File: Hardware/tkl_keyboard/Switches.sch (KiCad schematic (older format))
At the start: 178 parts, among them SW10 K33, SW11 K49, SW12 K64, SW13 K2, SW14 K18, SW15 K34, SW16 K50, SW17 K65, SW18 K78, SW19 K3, SW2 K0, SW20 K19, SW21 K35, SW22 K51, SW23 K66, SW24 K4, SW25 K20, SW26 K36, SW27 K52, SW28 K67, SW29 K79, SW3 K16, SW30 K5, SW31 K21, SW32 K37, SW33 K53, SW34 K68, SW35 K6, SW36 K22, SW37 K38, SW38 K54, SW39 K69, SW4 K32, SW40 K80, SW41 K7, SW42 K23, SW43 K39, SW44 K55, SW45 K70, SW46 K8, SW47 K24, SW48 K40, SW49 K56, SW5 K48, SW50 K71, SW51 K81, SW52 K9, SW53 K25, SW54 K41, SW55 K57, SW56 K72, SW57 K82, SW58 K10, SW59 K26, SW6 K63, SW60 K42, SW61 K58, SW62 K73, SW63 K83, SW64 K11, SW65 K27, SW66 K43, SW67 K59, SW68 K74, SW69 K84, SW7 K77, SW70 K12, SW71 K28, SW72 K44, SW73 K60, SW74 K75, SW75 K85, SW76 K13, SW77 K29, SW78 K45, SW79 K61, SW8 K1, SW80 K86, SW81 K14, SW82 K30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

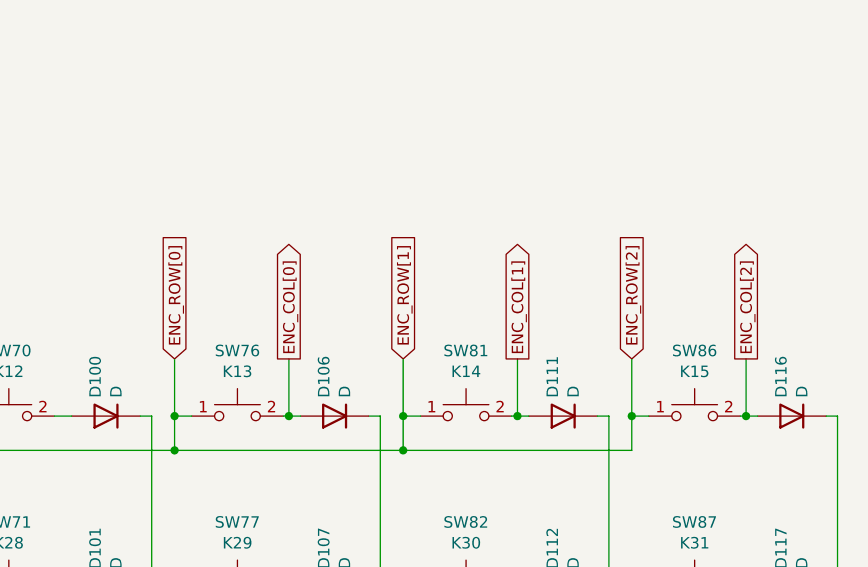
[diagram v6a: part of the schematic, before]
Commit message: Tidying schematic
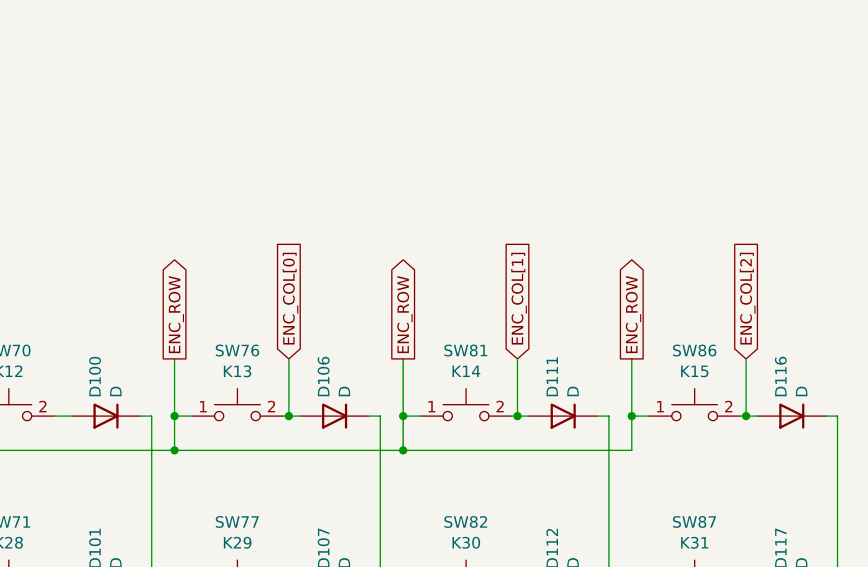
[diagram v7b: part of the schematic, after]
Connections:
- net ENC_ROW[0] renamed ENC_ROW
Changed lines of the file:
@@
 encoding utf-8
 Sheet 5 12
-Title ""
+Title "TKL Keyboard"
 Date ""
-Rev ""
+Rev "0"
 Comp ""
 Comment1 ""
@@
 $EndComp
 $Comp
-L Device:D D32
-U 1 1 61805335
-P 4675 5025
-AR Path="/62F5643B/61805335" Ref="D32"  Part="1"
-AR Path="/63013830/61805335" Ref="D?"  Part="1"
-AR Path="/6301FD9D/61805335" Ref="D?"  Part="1"
-F 0 "D32" V 4721 4945 50  0000 R CNN
-F 1 "D" V 4630 4945 50  0000 R CNN
-F 2 "custom_footprint_library:SOD323_HS" H 4675 5025 50  0001 C CNN
-F 3 "~" H 4675 5025 50  0001 C CNN
-	1    4675 5025
-	-1   0    0    1
-$EndComp
-$Comp
 L Device:D D38
 U 1 1 6180533B
@@
 	1    0    0    -1
 $EndComp
-Text GLabel 16975 4775 1    50   Input ~ 0
-ENC_ROW[0]
-Text GLabel 17475 4775 1    50   Output ~ 0
+Text GLabel 16975 4775 1    50   Output ~ 0
+ENC_ROW
+Text GLabel 17475 4775 1    50   Input ~ 0
 ENC_COL[0]
 Wire Wire Line
@@
 Wire Wire Line
 	17475 4775 17475 5025
-Text GLabel 17975 4775 1    50   Input ~ 0
-ENC_ROW[1]
-Text GLabel 18475 4775 1    50   Output ~ 0
+Text GLabel 18475 4775 1    50   Input ~ 0
 ENC_COL[1]
 Wire Wire Line
 	18475 4775 18475 5025
-Text GLabel 18975 4775 1    50   Input ~ 0
-ENC_ROW[2]
-Text GLabel 19475 4775 1    50   Output ~ 0
+Text GLabel 19475 4775 1    50   Input ~ 0
 ENC_COL[2]
 Wire Wire Line
@@
 Wire Wire Line
 	4975 8925 5975 8925
+$Comp
+L Device:D D32
+U 1 1 61805335
+P 4675 5025
+AR Path="/62F5643B/61805335" Ref="D32"  Part="1"
+AR Path="/63013830/61805335" Ref="D?"  Part="1"
+AR Path="/6301FD9D/61805335" Ref="D?"  Part="1"
+F 0 "D32" V 4721 4945 50  0000 R CNN
+F 1 "D" V 4630 4945 50  0000 R CNN
+F 2 "custom_footprint_library:SOD323_HS" H 4675 5025 50  0001 C CNN
+F 3 "~" H 4675 5025 50  0001 C CNN
+	1    4675 5025
+	-1   0    0    1
+$EndComp
+Text GLabel 17975 4775 1    50   Output ~ 0
+ENC_ROW
+Text GLabel 18975 4775 1    50   Output ~ 0
+ENC_ROW
 $EndSCHEMATC
